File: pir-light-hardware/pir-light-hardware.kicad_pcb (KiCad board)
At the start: 2 copper layers, 34.4 x 34.4 mm, 39 parts, among them J1 ZH1.5-3, J2 ZH1.5-3, Q1 DTC114EUA-TP, Q2 AON7240, Q3 DTA114EUAHE3-TP, Q7 DTA114EUAHE3-TP, U2 M74VHC1GT08DFT2G, U3 LMV331IDCKR, U4 LMV331IDCKR

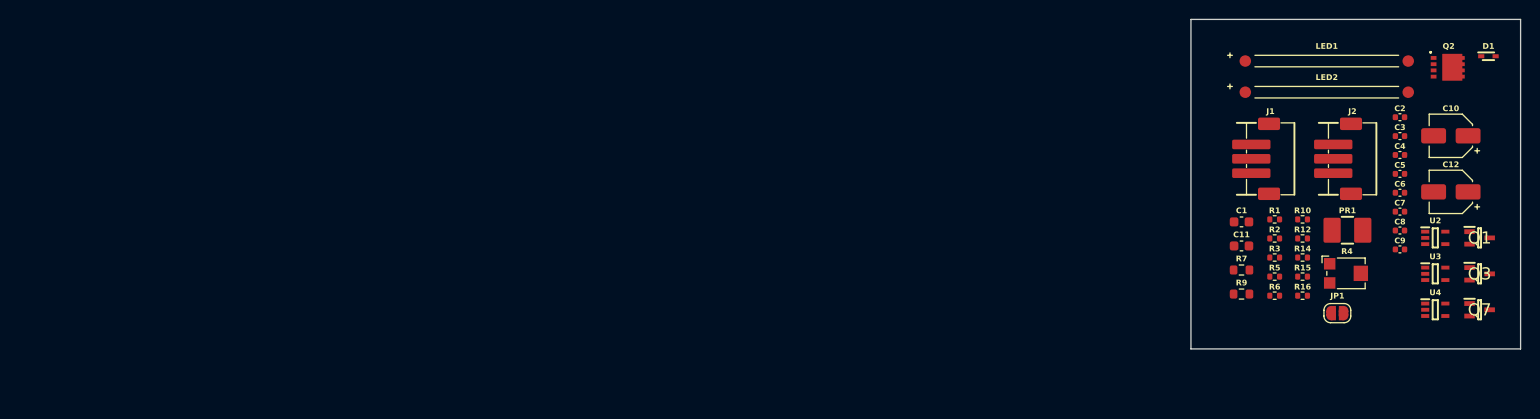
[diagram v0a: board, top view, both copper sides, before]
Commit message: chore: mark general PCB dimensions
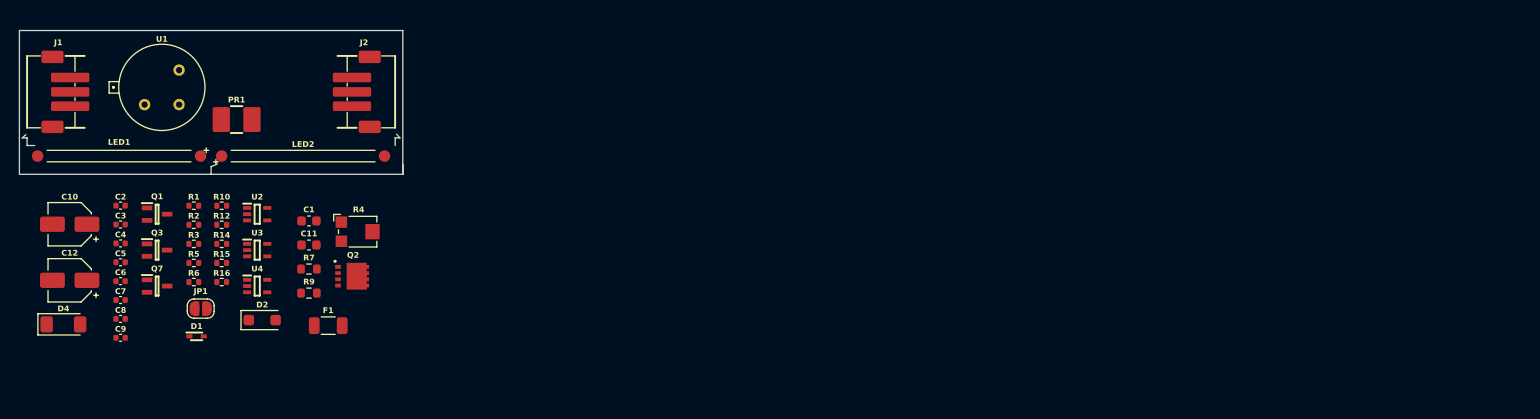
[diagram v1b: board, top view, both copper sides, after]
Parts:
- added D2: 1N5819, REST:D_SOD-123F, F.Cu at (79.5, 108.6)
- added D4: ZMM5V1, REST:D_MiniMELF, F.Cu at (58.8, 109.0)
- added F1: 100mA, REST:R_1206_3216Metric, F.Cu at (86.4, 109.2)
- added U1: AS312, AS312:AS312-NEW, F.Cu at (69.1, 84.3)
- moved C10 144.4 mm to (59.5, 98.6)
- moved C12 144.4 mm to (59.5, 104.5)
- moved Q1 138.0 mm to (68.6, 97.5)
- moved Q3 138.0 mm to (68.6, 101.3)
- moved Q7 138.0 mm to (68.6, 105.0)
- moved D1 137.9 mm to (72.7, 110.3)
- moved C2 133.8 mm to (64.8, 96.7)
- moved C3 133.8 mm to (64.8, 98.6)
- moved C4 133.8 mm to (64.8, 100.6)
- moved C5 133.8 mm to (64.8, 102.6)
- moved C6 133.8 mm to (64.8, 104.5)
- moved C7 133.8 mm to (64.8, 106.5)
- moved C8 133.8 mm to (64.8, 108.5)
- moved C9 133.8 mm to (64.8, 110.5)
- moved J1 127.4 mm to (57.5, 84.8), turned to 180 degrees
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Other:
- board size 34.4 x 34.4 mm -> 40 x 15 mm

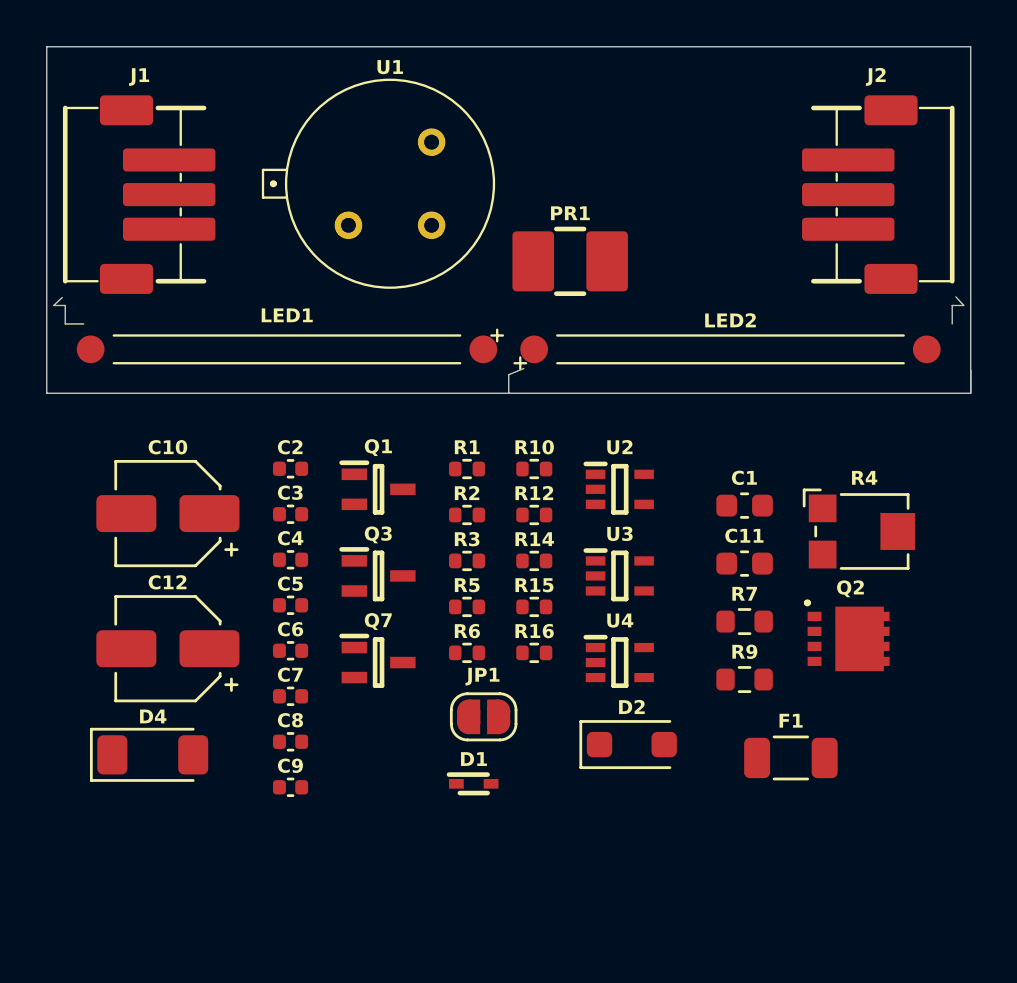
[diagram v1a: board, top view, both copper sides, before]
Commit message: chore: add top pcb layout
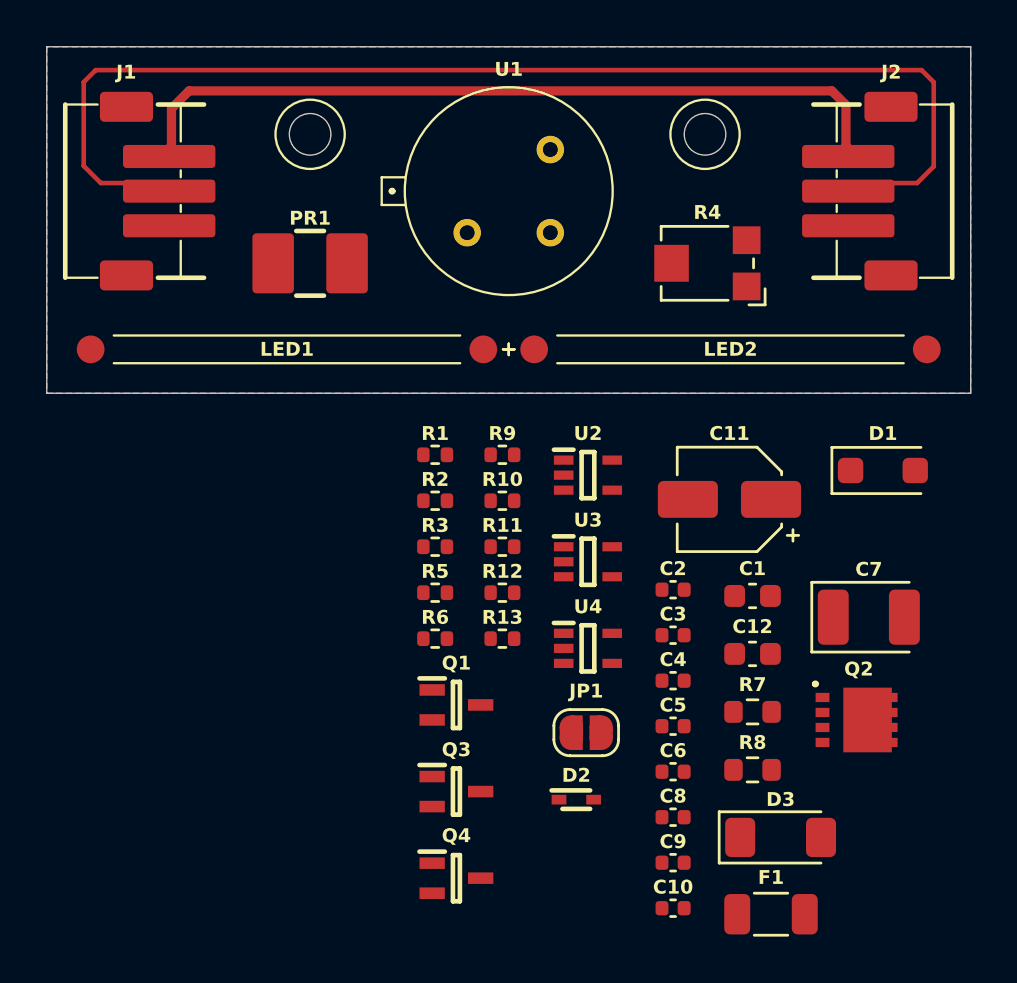
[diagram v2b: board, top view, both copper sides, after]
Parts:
- removed D4: ZMM5V1, REST:D_MiniMELF
- removed Q7: DTA114EUAHE3-TP, DTA114EUAHE3-TP:SOT65P228X120-3N
- removed R14: 47kR, REST:R_0402_1005Metric
- removed R15, R16: 1MR, REST:R_0402_1005Metric
- added D3: ZMM5V1, REST:D_MiniMELF, F.Cu at (86.0, 112.6)
- added Q4: DTC114EUA-TP, DTC114EUA-TP:SOT65P228X120-3N, F.Cu at (71.9, 114.4)
- added R11: 47kR, REST:R_0402_1005Metric, F.Cu at (73.9, 100.0)
- added R13: 1MR, REST:R_0402_1005Metric, F.Cu at (73.9, 104.0)
- added R8: 0R, REST:R_0603_1608Metric, F.Cu at (84.8, 109.7)
- C10: value 33uF -> 100nF; footprint REST:CP_Elec_4x5.4 -> REST:C_0402_1005Metric
- C11: value 10uF -> 33uF; footprint REST:C_0603_1608Metric -> REST:CP_Elec_4x5.4
- C12: value 47uF -> 10uF; footprint REST:CP_Elec_4x5.4 -> REST:C_0603_1608Metric
- C7: value 100nF -> 47uF; footprint REST:C_0402_1005Metric -> REST:CP_EIA-3528-12_Kemet-T
- D1: value 1N5819HWQ-7-F -> 1N5819; footprint 1N5819HWQ-7-F:1N5819HWQ-7-F -> REST:D_SOD-123F
- D2: value 1N5819 -> 1N5819HWQ-7-F; footprint REST:D_SOD-123F -> 1N5819HWQ-7-F:1N5819HWQ-7-F
- Q1: value DTC114EUA-TP -> DTA114EUAHE3-TP; footprint DTC114EUA-TP:SOT65P228X120-3N -> DTA114EUAHE3-TP:SOT65P228X120-3N
- R10: value 10kR -> 620kR
- R12: value 620kR -> 1MR
- R9: value 0R -> 10kR; footprint REST:R_0603_1608Metric -> REST:R_0402_1005Metric
- moved C10 27.8 mm to (81.3, 115.7)
- moved C12 25.3 mm to (84.8, 104.7)
- moved C7 25.3 mm to (89.8, 103.1)
- moved D1 22.3 mm to (90.4, 96.7)
- moved C5 17.4 mm to (81.3, 107.8)
- moved C2 17.4 mm to (81.3, 101.9)
- moved C3 17.4 mm to (81.3, 103.9)
- moved C4 17.4 mm to (81.3, 105.8)
- moved C6 17.4 mm to (81.3, 109.8)
- moved C8 16.9 mm to (81.3, 111.7)
- moved C9 16.9 mm to (81.3, 113.7)
- moved R9 14.3 mm to (73.9, 96.1)
- moved R4 13.5 mm to (82.7, 87.8), turned to 180 degrees
- moved PR1 11.3 mm to (65.6, 87.8)
- moved Q1 9.92 mm to (71.9, 106.9)
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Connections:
- C10 pad 1: Net-(Q3-OUT) -> 3V3
- C11 pad 1: /FB -> Net-(Q1-OUT)
- C12 pad 1: 3V3 -> /FB
- C4 pad 1: 3V3 -> /ALT
- C5 pad 1: /ALT -> /ALV
- C6 pad 1: /ALV -> /FBT
- C7 pad 1: /FBT -> 3V3
- D1 pad 1: /STL -> 3V3
- D1 pad 2: Net-(D1-A) -> GND
- D2 pad 1: 3V3 -> /STL
- D2 pad 2: GND -> Net-(D2-A)
- J1 pad 2: VIN -> /STL
- J1 pad 3: /STL -> VIN
- J2 pad 1: /STL -> VIN
- J2 pad 2: VIN -> /STL
- Q1 pad 1: /STL -> Net-(Q1-IN)
- Q1 pad 2: GND -> 3V3
- Q3 pad 1: Net-(Q1-OUT) -> Net-(Q3-IN)
- Q3 pad 2: 3V3 -> Net-(Q3-GND)
- R10 pad 1: 3V3 -> Net-(Q1-OUT)
- R10 pad 2: Net-(Q7-GND) -> /FB
- R12 pad 1: Net-(Q3-OUT) -> Net-(Q1-OUT)
- R12 pad 2: /FB -> GND
- R9 pad 2: Net-(LED2-Pad1) -> Net-(Q3-GND)
- U2 pad 1: Net-(Q7-GND) -> Net-(Q3-GND)
- U2 pad 4: Net-(D1-A) -> Net-(D2-A)
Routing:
- net /STL: track 0.00 -> 52.0 mm
- net VIN: track 0.00 -> 33.5 mm
- added copper zone on B.Cu, net GND
- added copper zone on F.Cu, net GND
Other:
- outline, holes or cut-outs redrawn
